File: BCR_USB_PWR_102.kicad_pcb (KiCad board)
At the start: 2 copper layers, 22.2 x 13.3 mm, 2 parts, among them CN1 DB9_Female, CN2 UE27AC54100

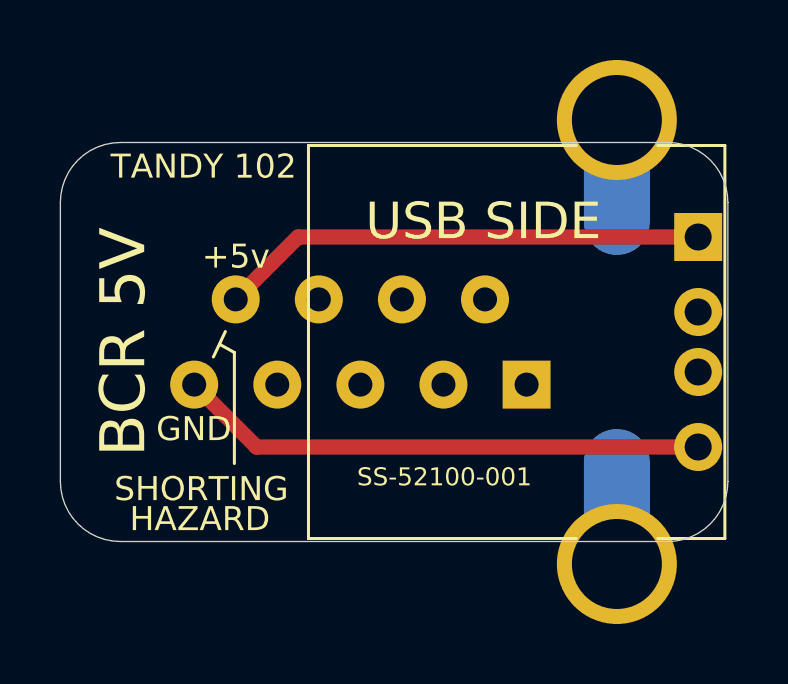
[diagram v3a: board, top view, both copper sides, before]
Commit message: db9 pin 7 is the real GND, not pin 5
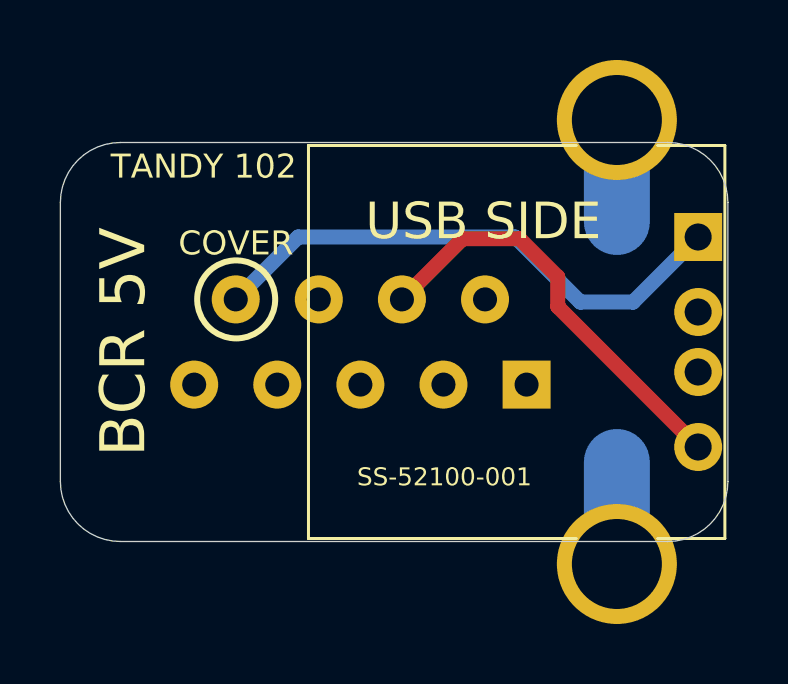
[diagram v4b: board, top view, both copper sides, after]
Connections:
- CN1 pad 5: /GND -> (no net)
- CN1 pad 7: (no net) -> /GND
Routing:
- net /GND: track 17.7 -> 14.2 mm
- net /+5V: track 16.3 -> 18.1 mm
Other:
- net class Default: clearance 0.2 -> 0.16; trace_width 0.25 -> 0.16; via_dia 0.8 -> 0.42; via_drill 0.4 -> 0.26
- rule trace_clearance: 0.2 -> 0.16
- rule trace_min: 0.2 -> 0.16
- rule via_min_drill: 0.3 -> 0.26
- rule via_min_size: 0.4 -> 0.42
- board text added: "COVER"
- board text removed: "+5v"
- board text removed: "GND"
- board text removed: "HAZARD"
- board text removed: "SHORTING"
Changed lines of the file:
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@@
   (general
     (thickness 1.6)
-    (drawings 30)
-    (tracks 4)
+    (drawings 25)
+    (tracks 10)
     (zones 0)
     (modules 2)
@@
   )
   (setup
-    (last_trace_width 0.25)
-    (user_trace_width 0.508)
-    (trace_clearance 0.2)
+    (last_trace_width 0.5)
+    (user_trace_width 0.5)
+    (trace_clearance 0.16)
     (zone_clearance 0.508)
     (zone_45_only no)
-    (trace_min 0.2)
-    (via_size 0.8)
-    (via_drill 0.4)
-    (via_min_size 0.4)
-    (via_min_drill 0.3)
-    (user_via 0.508 0.3048)
+    (trace_min 0.16)
+    (via_size 0.42)
+    (via_drill 0.26)
+    (via_min_size 0.42)
+    (via_min_drill 0.26)
     (uvia_size 0.3)
     (uvia_drill 0.1)
@@
     (mod_text_size 1 1)
     (mod_text_width 0.15)
-    (pad_size 1.524 1.524)
-    (pad_drill 0.762)
+    (pad_size 1.6 1.6)
+    (pad_drill 0.8)
     (pad_to_mask_clearance 0)
     (aux_axis_origin 0 0)
@@
   (net 3 "Net-(CN2-PadSH)")
   (net_class Default "This is the default net class."
-    (clearance 0.2)
-    (trace_width 0.25)
-    (via_dia 0.8)
-    (via_drill 0.4)
+    (clearance 0.16)
+    (trace_width 0.16)
+    (via_dia 0.42)
+    (via_drill 0.26)
     (uvia_dia 0.3)
     (uvia_drill 0.1)
@@
       (effects (font (size 1 1) (thickness 0.15)) (justify mirror))
     )
-    (fp_text user %R (at -5.54 -1.42) (layer B.Fab)
-      (effects (font (size 1 1) (thickness 0.15)) (justify mirror))
-    )
-    (fp_arc (start -0.137048 -3.77) (end -0.137048 -5.43) (angle 80) (layer B.SilkS) (width 0.12))
-    (fp_arc (start -10.942952 -3.77) (end -10.942952 -5.43) (angle -80) (layer B.SilkS) (width 0.12))
-    (fp_arc (start 0.691689 0.93) (end 0.691689 2.59) (angle -100) (layer B.SilkS) (width 0.12))
-    (fp_arc (start -11.771689 0.93) (end -11.771689 2.59) (angle 100) (layer B.SilkS) (width 0.12))
-    (fp_arc (start -0.125543 -3.77) (end -0.125543 -5.37) (angle 80) (layer B.Fab) (width 0.1))
-    (fp_arc (start -10.954457 -3.77) (end -10.954457 -5.37) (angle -80) (layer B.Fab) (width 0.1))
-    (fp_arc (start 0.703194 0.93) (end 0.703194 2.53) (angle -100) (layer B.Fab) (width 0.1))
-    (fp_arc (start -11.783194 0.93) (end -11.783194 2.53) (angle 100) (layer B.Fab) (width 0.1))
     (fp_line (start -6.54 -1.42) (end -4.54 -1.42) (layer Dwgs.User) (width 0.01))
     (fp_line (start -5.54 -0.82) (end -5.54 -2.02) (layer Dwgs.User) (width 0.01))
@@
     (fp_line (start 2.9 -6.74) (end 2.9 3.91) (layer B.CrtYd) (width 0.05))
     (fp_line (start 2.9 3.91) (end -13.95 3.91) (layer B.CrtYd) (width 0.05))
+    (fp_text user %R (at -5.54 -1.42) (layer B.Fab)
+      (effects (font (size 1 1) (thickness 0.15)) (justify mirror))
+    )
+    (fp_arc (start -0.137048 -3.77) (end -0.137048 -5.43) (angle 80) (layer B.SilkS) (width 0.12))
+    (fp_arc (start -10.942952 -3.77) (end -10.942952 -5.43) (angle -80) (layer B.SilkS) (width 0.12))
+    (fp_arc (start 0.691689 0.93) (end 0.691689 2.59) (angle -100) (layer B.SilkS) (width 0.12))
+    (fp_arc (start -11.771689 0.93) (end -11.771689 2.59) (angle 100) (layer B.SilkS) (width 0.12))
+    (fp_arc (start -0.125543 -3.77) (end -0.125543 -5.37) (angle 80) (layer B.Fab) (width 0.1))
+    (fp_arc (start -10.954457 -3.77) (end -10.954457 -5.37) (angle -80) (layer B.Fab) (width 0.1))
+    (fp_arc (start 0.703194 0.93) (end 0.703194 2.53) (angle -100) (layer B.Fab) (width 0.1))
+    (fp_arc (start -11.783194 0.93) (end -11.783194 2.53) (angle 100) (layer B.Fab) (width 0.1))
     (pad 9 thru_hole circle (at -9.695 -2.84) (size 1.6 1.6) (drill 0.8) (layers *.Cu *.Mask)
       (net 1 /+5V))
     (pad 8 thru_hole circle (at -6.925 -2.84) (size 1.6 1.6) (drill 0.8) (layers *.Cu *.Mask))
-    (pad 7 thru_hole circle (at -4.155 -2.84) (size 1.6 1.6) (drill 0.8) (layers *.Cu *.Mask))
+    (pad 7 thru_hole circle (at -4.155 -2.84) (size 1.6 1.6) (drill 0.8) (layers *.Cu *.Mask)
+      (net 2 /GND))
     (pad 6 thru_hole circle (at -1.385 -2.84) (size 1.6 1.6) (drill 0.8) (layers *.Cu *.Mask))
-    (pad 5 thru_hole circle (at -11.08 0) (size 1.6 1.6) (drill 0.8) (layers *.Cu *.Mask)
-      (net 2 /GND))
+    (pad 5 thru_hole circle (at -11.08 0) (size 1.6 1.6) (drill 0.8) (layers *.Cu *.Mask))
     (pad 4 thru_hole circle (at -8.31 0) (size 1.6 1.6) (drill 0.8) (layers *.Cu *.Mask))
     (pad 3 thru_hole circle (at -5.54 0) (size 1.6 1.6) (drill 0.8) (layers *.Cu *.Mask))
@@
     )
     (fp_text value UE27AC54100 (at 0 11.35 270) (layer F.Fab)
-      (effects (font (size 1 1) (thickness 0.15)))
-    )
-    (fp_text user %R (at -0.025 0.975 270) (layer F.Fab)
       (effects (font (size 1 1) (thickness 0.15)))
     )
@@
     (fp_line (start -6.75 -3.94) (end -6.75 10.375) (layer F.CrtYd) (width 0.05))
     (fp_line (start -6.75 10.375) (end 6.75 10.375) (layer F.CrtYd) (width 0.05))
+    (fp_text user %R (at -0.025 0.975 270) (layer F.Fab)
+      (effects (font (size 1 1) (thickness 0.15)))
+    )
     (pad SH smd oval (at 6.8 0 270) (size 4.8 2.2) (drill (offset -1.5 0)) (layers B.Cu B.Paste B.Mask)
       (net 3 "Net-(CN2-PadSH)"))
@@
     )
   )
+  (gr_circle (center 122.86 94.338) (end 124.16 94.338) (layer F.SilkS) (width 0.2))
   (gr_arc (start 137.25 91.108) (end 139.25 91.108) (angle -90) (layer Edge.Cuts) (width 0.025))
   (gr_arc (start 137.25 100.408) (end 137.25 102.408) (angle -90) (layer Edge.Cuts) (width 0.025))
@@
   (gr_line (start 139.25 100.408) (end 139.25 91.108) (layer Edge.Cuts) (width 0.025))
   (gr_line (start 137.25 102.408) (end 119 102.408) (layer Edge.Cuts) (width 0.025))
-  (gr_line (start 122.1 96.258) (end 122.5 95.408) (layer F.SilkS) (width 0.1016))
-  (gr_line (start 122.8 96.108) (end 122.35 95.858) (layer F.SilkS) (width 0.1016))
-  (gr_line (start 122.8 99.808) (end 122.8 96.108) (layer F.SilkS) (width 0.1016))
-  (gr_text SHORTING (at 121.7 100.658) (layer F.SilkS)
-    (effects (font (size 0.8 0.8) (thickness 0.08)))
-  )
-  (gr_text HAZARD (at 121.65 101.658) (layer F.SilkS)
-    (effects (font (size 0.8 0.8) (thickness 0.08)))
-  )
-  (gr_text +5v (at 122.85 92.908) (layer F.SilkS)
-    (effects (font (size 0.8 0.8) (thickness 0.15)))
-  )
-  (gr_text GND (at 121.45 98.658) (layer F.SilkS)
-    (effects (font (size 0.8 0.8) (thickness 0.15)))
+  (gr_text COVER (at 122.85 92.468) (layer F.SilkS)
+    (effects (font (size 0.8 0.8) (thickness 0.1)))
   )
   (gr_text "TANDY 102" (at 121.775 89.908) (layer F.SilkS)
@@
     (effects (font (size 1.2192 1.2192) (thickness 0.2032)))
   )
-  (segment (start 124.925 92.258) (end 122.845 94.338) (width 0.508) (layer F.Cu) (net 1))
-  (segment (start 138.26 92.258) (end 124.925 92.258) (width 0.508) (layer F.Cu) (net 1))
-  (segment (start 123.54 99.258) (end 121.46 97.178) (width 0.508) (layer F.Cu) (net 2))
-  (segment (start 138.26 99.258) (end 123.54 99.258) (width 0.508) (layer F.Cu) (net 2))
+  (segment (start 124.925 92.258) (end 122.845 94.338) (width 0.5) (layer B.Cu) (net 1))
+  (segment (start 124.925 92.258) (end 132.16 92.258) (width 0.5) (layer B.Cu) (net 1))
+  (segment (start 132.16 92.258) (end 134.33 94.428) (width 0.5) (layer B.Cu) (net 1))
+  (segment (start 136.09 94.428) (end 138.26 92.258) (width 0.5) (layer B.Cu) (net 1))
+  (segment (start 134.33 94.428) (end 136.09 94.428) (width 0.5) (layer B.Cu) (net 1))
+  (segment (start 132.31 92.318) (end 130.405 92.318) (width 0.5) (layer F.Cu) (net 2))
+  (segment (start 133.58 93.588) (end 132.31 92.318) (width 0.5) (layer F.Cu) (net 2))
+  (segment (start 130.405 92.318) (end 128.385 94.338) (width 0.5) (layer F.Cu) (net 2))
+  (segment (start 138.26 99.258) (end 133.58 94.578) (width 0.5) (layer F.Cu) (net 2))
+  (segment (start 133.58 94.578) (end 133.58 93.588) (width 0.5) (layer F.Cu) (net 2))
 )
